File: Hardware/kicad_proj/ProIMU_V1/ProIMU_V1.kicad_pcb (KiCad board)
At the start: 2 copper layers, 50 x 50 mm, 40 parts, among them J1 USB4105-GF-A, J2 502570-0893, J3 Conn_01x01, J4 Conn_01x01, J5 Conn_01x01, J6 Conn_01x01, J7 Conn_01x01, U1 BMP280, U11 TJA1051T-3, U2 MPU-9250, U3 STM32F412CEU6, U4 AIR602

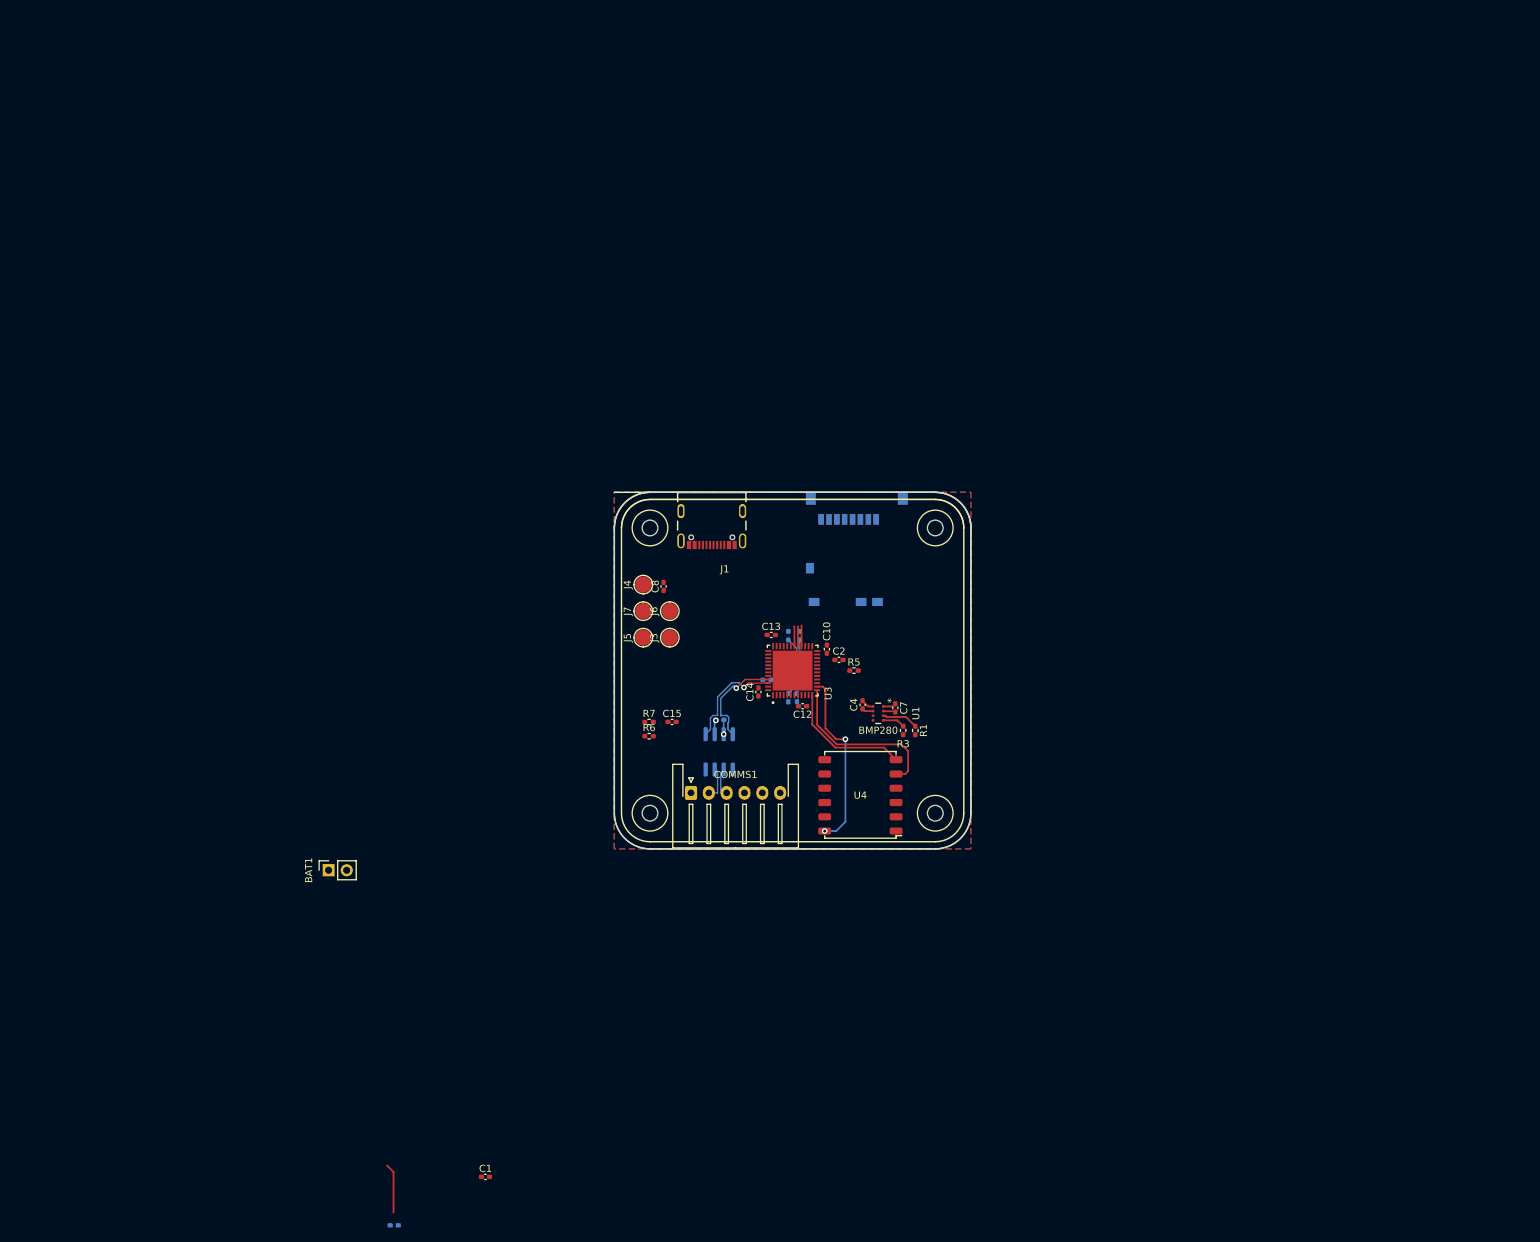
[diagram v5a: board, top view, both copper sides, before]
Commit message: Layout Updated. CAN and RS485 section to be updated
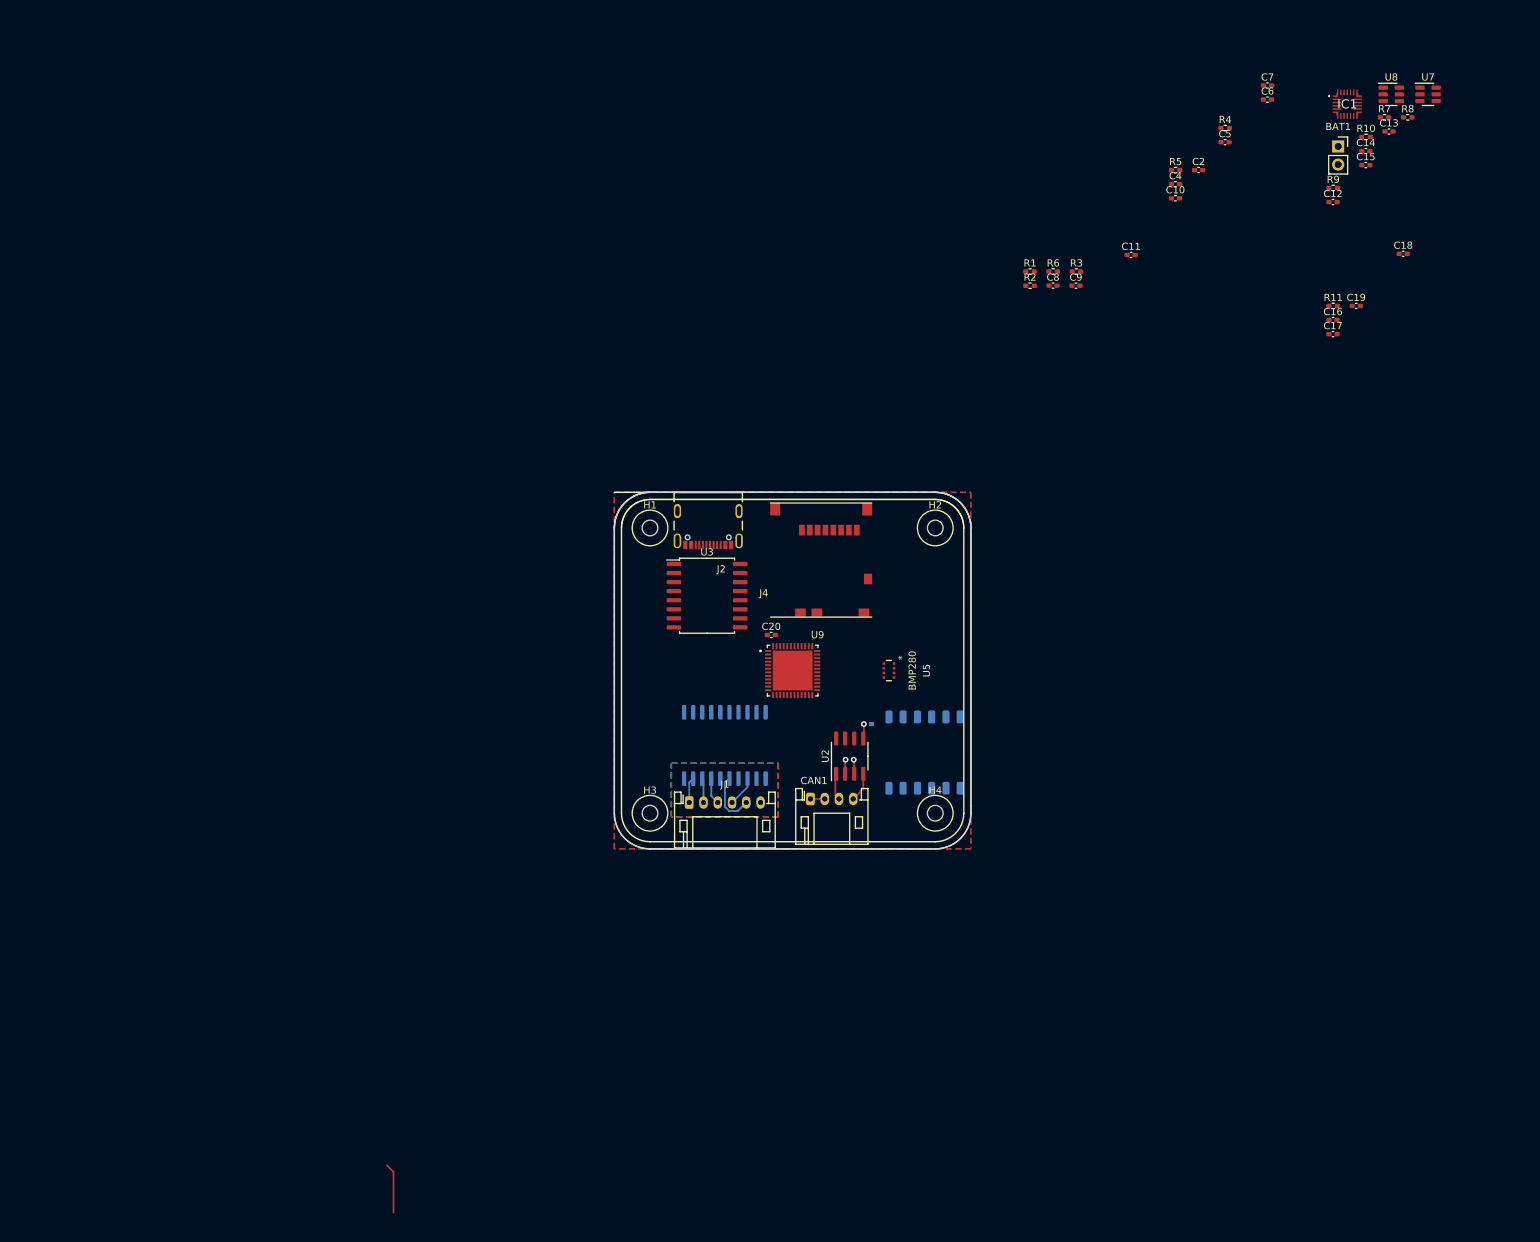
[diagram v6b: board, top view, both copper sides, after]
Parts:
- removed COMMS1: Conn_01x06, Connector_JST:JST_XH_S6B-XH-A-1_1x06_P2.50mm_Horizontal
- removed J3, J5, J6, J7: Conn_01x01, footprints:Test_Point
- removed U11: TJA1051T-3, Package_SO:SOIC-8_3.9x4.9mm_P1.27mm
- added C16: 1uF, Capacitor_SMD:C_0402_1005Metric_Pad0.74x0.62mm_HandSolder, F.Cu at (224.3, 55.9)
- added C17: 1uF, Capacitor_SMD:C_0402_1005Metric_Pad0.74x0.62mm_HandSolder, F.Cu at (224.3, 57.8)
- added C18: 1uF, Capacitor_SMD:C_0402_1005Metric_Pad0.74x0.62mm_HandSolder, F.Cu at (234.1, 46.5)
- added C19: 1uF, Capacitor_SMD:C_0402_1005Metric_Pad0.74x0.62mm_HandSolder, F.Cu at (227.5, 53.9)
- added C20: 1uF, Capacitor_SMD:C_0402_1005Metric_Pad0.74x0.62mm_HandSolder, F.Cu at (145.5, 100.0)
- added CAN1: Conn_02x02_Counter_Clockwise, Connector_JST:JST_PH_S4B-PH-K_1x04_P2.00mm_Horizontal, F.Cu at (151.0, 123.0)
- added IC1: MP2731GQC-0000-Z, footprints:MP2731GQC0000Z, F.Cu at (226.3, 25.6)
- added R10: 10K, Resistor_SMD:R_0402_1005Metric_Pad0.72x0.64mm_HandSolder, F.Cu at (228.9, 30.2)
- added R11: 10K, Resistor_SMD:R_0402_1005Metric_Pad0.72x0.64mm_HandSolder, F.Cu at (224.3, 53.9)
- added R8: 10K, Resistor_SMD:R_0402_1005Metric_Pad0.72x0.64mm_HandSolder, F.Cu at (234.8, 27.4)
- added R9: 10K, Resistor_SMD:R_0402_1005Metric_Pad0.72x0.64mm_HandSolder, F.Cu at (224.3, 37.3)
- added U5: BMP280, footprints:BMP280, F.Cu at (162.0, 105.0)
- added U6: MPU-9250, footprints:QFN40P300X300X105-24N, B.Cu at (148.5, 105.0)
- added U7: TPS54308, Package_TO_SOT_SMD:SOT-23-6, F.Cu at (237.6, 24.2)
- added U8: TPS54308, Package_TO_SOT_SMD:SOT-23-6, F.Cu at (232.4, 24.2)
- added U9: STM32F412CEU6, footprints:QFN50P700X700X60-49N, F.Cu at (148.5, 105.0)
- C1, U4: moved to B.Cu
- C10: value 1uF -> 100nF
- C11: value 1uF -> 10nF; moved to F.Cu
- C3: value 0.1uF -> 1uF
- C4: value 100nF -> 1uF
- C5: value 10nF -> 1uF; moved to F.Cu
- C6: value 0.1uF -> 100nF; moved to F.Cu
- C7: value 100nF -> 0.1uF
- C8: value 1uF -> 0.1uF
- C9, R2, R4: moved to F.Cu
- J1: value USB4105-GF-A -> Conn_01x06; footprint footprints:GCT_USB4105-GF-A -> Connector_JST:JST_PH_S6B-PH-K_1x06_P2.00mm_Horizontal
- J2: value 502570-0893 -> USB4105-GF-A; footprint footprints:MOLEX_502570-0893 -> footprints:GCT_USB4105-GF-A; moved to F.Cu
- J4: value Conn_01x01 -> 502570-0893; footprint footprints:Test_Point -> footprints:MOLEX_502570-0893
- R5: value 10K -> 2.2K
- R7: value 2.2K -> 10K
- U1: value BMP280 -> ADM2582E; footprint footprints:BMP280 -> Package_SO:SOIC-20W_7.5x12.8mm_P1.27mm; moved to B.Cu
- U2: value MPU-9250 -> TJA1051T-3; footprint footprints:QFN40P300X300X105-24N -> Package_SO:SOIC-8_3.9x4.9mm_P1.27mm; moved to F.Cu
- U3: value STM32F412CEU6 -> ADUM3160; footprint footprints:QFN50P700X700X60-49N -> Package_SO:SOIC-16W_7.5x10.3mm_P1.27mm
- moved BAT1 174.2 mm to (225.0, 31.5), turned to 0 degrees
- moved C9 162.8 mm to (188.2, 51.0)
- moved R7 133.5 mm to (231.5, 27.4)
- moved C15 124.7 mm to (228.9, 34.1)
- moved C14 114.1 mm to (228.9, 32.1), turned to 0 degrees
- moved C13 111.8 mm to (232.1, 29.4)
- moved C6 107.5 mm to (215.1, 24.9), turned to 0 degrees
- moved C12 102.6 mm to (224.3, 39.3), turned to 0 degrees
- moved C7 101.7 mm to (215.1, 23.0), turned to 0 degrees
- moved C5 98.4 mm to (209.1, 30.9), turned to 0 degrees
- moved R4 92.9 mm to (209.2, 28.9), turned to 0 degrees
- moved C11 87.0 mm to (196.0, 46.7), turned to 0 degrees
- moved R6 86.4 mm to (185.0, 49.0)
- moved C2 85.2 mm to (205.4, 34.8), turned to 0 degrees
- moved C4 85.2 mm to (202.2, 36.8), turned to 0 degrees
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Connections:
- C1 pad 1: +5V -> GND
- C1 pad 2: GND -> +3V3
- C11 pad 1: +5V -> +3V3
- C12 pad 1: +3V3 -> Net-(C12-Pad1)
- C12 pad 2: GND -> Net-(C12-Pad2)
- C13 pad 1: +3V3 -> Net-(C13-Pad1)
- C13 pad 2: GND -> Net-(C13-Pad2)
- C15 pad 1: GND -> +5V
- C15 pad 2: Net-(C15-Pad2) -> GND
- C2 pad 1: Net-(C2-Pad1) -> GND
- C2 pad 2: GND -> VDD
- C3 pad 1: +5V -> GND
- C3 pad 2: GND -> +5V
- C4 pad 1: +5V -> GND
- C4 pad 2: GND -> +3V3
- C5 pad 1: +3V3 -> GND
- C5 pad 2: GND -> Net-(C5-Pad2)
- C6 pad 1: Net-(C6-Pad1) -> GND
- C6 pad 2: GND -> +3V3
- C7 pad 1: +3V3 -> +5V
- C8 pad 1: +5V -> Net-(C8-Pad1)
- C9 pad 1: GND -> +5V
- C9 pad 2: +3V3 -> GND
- J4 pad 1: /SWCLK -> /MCU/SDCARD_D2
- R1 pad 1: /BMP280_SCL -> /MCU/CAN_L
- R1 pad 2: +3V3 -> Net-(C5-Pad2)
- R2 pad 1: /MPU9250_SCK -> Net-(C5-Pad2)
- R2 pad 2: +3V3 -> /MCU/CAN_H
- R3 pad 1: /BMP280_SDA -> /MCU/MPU9250_SDA
- R4 pad 1: /MPU9250_SDA -> /MCU/MPU9250_SCK
- R5 pad 1: +3V3 -> /MCU/BMP280_SCK
- R5 pad 2: Net-(R5-Pad2) -> +3V3
- R6 pad 1: Net-(C15-Pad2) -> /MCU/BMP280_SDA
- R6 pad 2: /CAN+ -> +3V3
- R7 pad 1: /CAN- -> Net-(R7-Pad1)
- R7 pad 2: Net-(C15-Pad2) -> +3V3
- U1 pad 3: /BMP280_SCL -> GND
- U1 pad 4: /BMP280_SDA -> /MCU/RS485_RXD
- U1 pad 5: GND -> /MCU/RS485_nRE
- U1 pad 6: +3V3 -> /MCU/RS485_DE
- U1 pad 7: GND -> /MCU/RS485_TXD
- U1 pad 8: +5V -> +3V3
- U2 pad 1: +3V3 -> Net-(CAN1-Pad3)
- U2 pad 2: (no net) -> GND
- U2 pad 3: (no net) -> +5V
- U2 pad 4: (no net) -> Net-(CAN1-Pad4)
- U2 pad 5: (no net) -> +3V3
- U2 pad 6: (no net) -> /MCU/CAN_L
- U2 pad 7: unconnected-(U2-Pad7) -> /MCU/CAN_H
- U2 pad 8: +3V3 -> /MCU/CAN_SHUTDOWN
- U3 pad 1: +BATT -> VDD
- U3 pad 10: unconnected-(U3-Pad10) -> /MCU/D+
- U3 pad 11: unconnected-(U3-Pad11) -> /MCU/D-
- U3 pad 12: /WIFI_UART_TX -> /MCU/PIN
- U3 pad 13: /WIFI_UART_RX -> /MCU/SPD
- U3 pad 14: /WIFI_RES -> +3V3
- U3 pad 15: unconnected-(U3-Pad15) -> GND
- U3 pad 16: /SDCARD_CMD -> +3V3
- U3 pad 2: unconnected-(U3-Pad2) -> Net-(J2-PadA1_B12)
- U3 pad 3: unconnected-(U3-Pad3) -> VDD
- U3 pad 4: unconnected-(U3-Pad4) -> /MCU/SPU
- U3 pad 5: unconnected-(U3-Pad5) -> /MCU/PDEN
- U3 pad 6: unconnected-(U3-Pad6) -> Net-(J2-PadA7)
- U3 pad 7: /NRST -> Net-(J2-PadA6)
- U3 pad 8: GND -> Net-(J2-PadA1_B12)
- U3 pad 9: +3V3 -> GND
- U4 pad 12: /WIFI_RES -> /MCU/WIFI_RESET
- U4 pad 5: /WIFI_UART_RX -> /MCU/WIFI_UART_TX
- U4 pad 6: /WIFI_UART_TX -> /MCU/WIFI_UART_RX
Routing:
- net /WIFI_RES: track 25.3 -> 0.00 mm, vias 2 -> 0
- net /WIFI_UART_RX: track 23.8 -> 0.00 mm
- net /WIFI_UART_TX: track 17.9 -> 0.00 mm
- net /CAN_TRX+: track 14.7 -> 0.00 mm, vias 1 -> 0
- net /CAN_TRX-: track 14.4 -> 0.00 mm, vias 1 -> 0
- net /SDCARD_CLK: track 9.89 -> 0.00 mm
- net Net-(J1-Pad5): track 0.00 -> 7.95 mm
- net (no net): track 0.00 -> 6.97 mm
- net /BMP280_SCL: track 5.09 -> 0.00 mm
- net /CAN+: track 4.64 -> 0.00 mm
- net Net-(J1-Pad4): track 0.00 -> 4.25 mm
- net /CAN-: track 4.24 -> 0.00 mm
- net Net-(CAN1-Pad4): track 0.00 -> 4.11 mm
- net Net-(CAN1-Pad3): track 0.00 -> 3.77 mm
- net Net-(J1-Pad3): track 0.00 -> 3.72 mm
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- added copper zone on B.Cu, net GND1
- added copper zone on F.Cu, net GND1

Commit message: Updated Schematic and Layout. Needs more refining
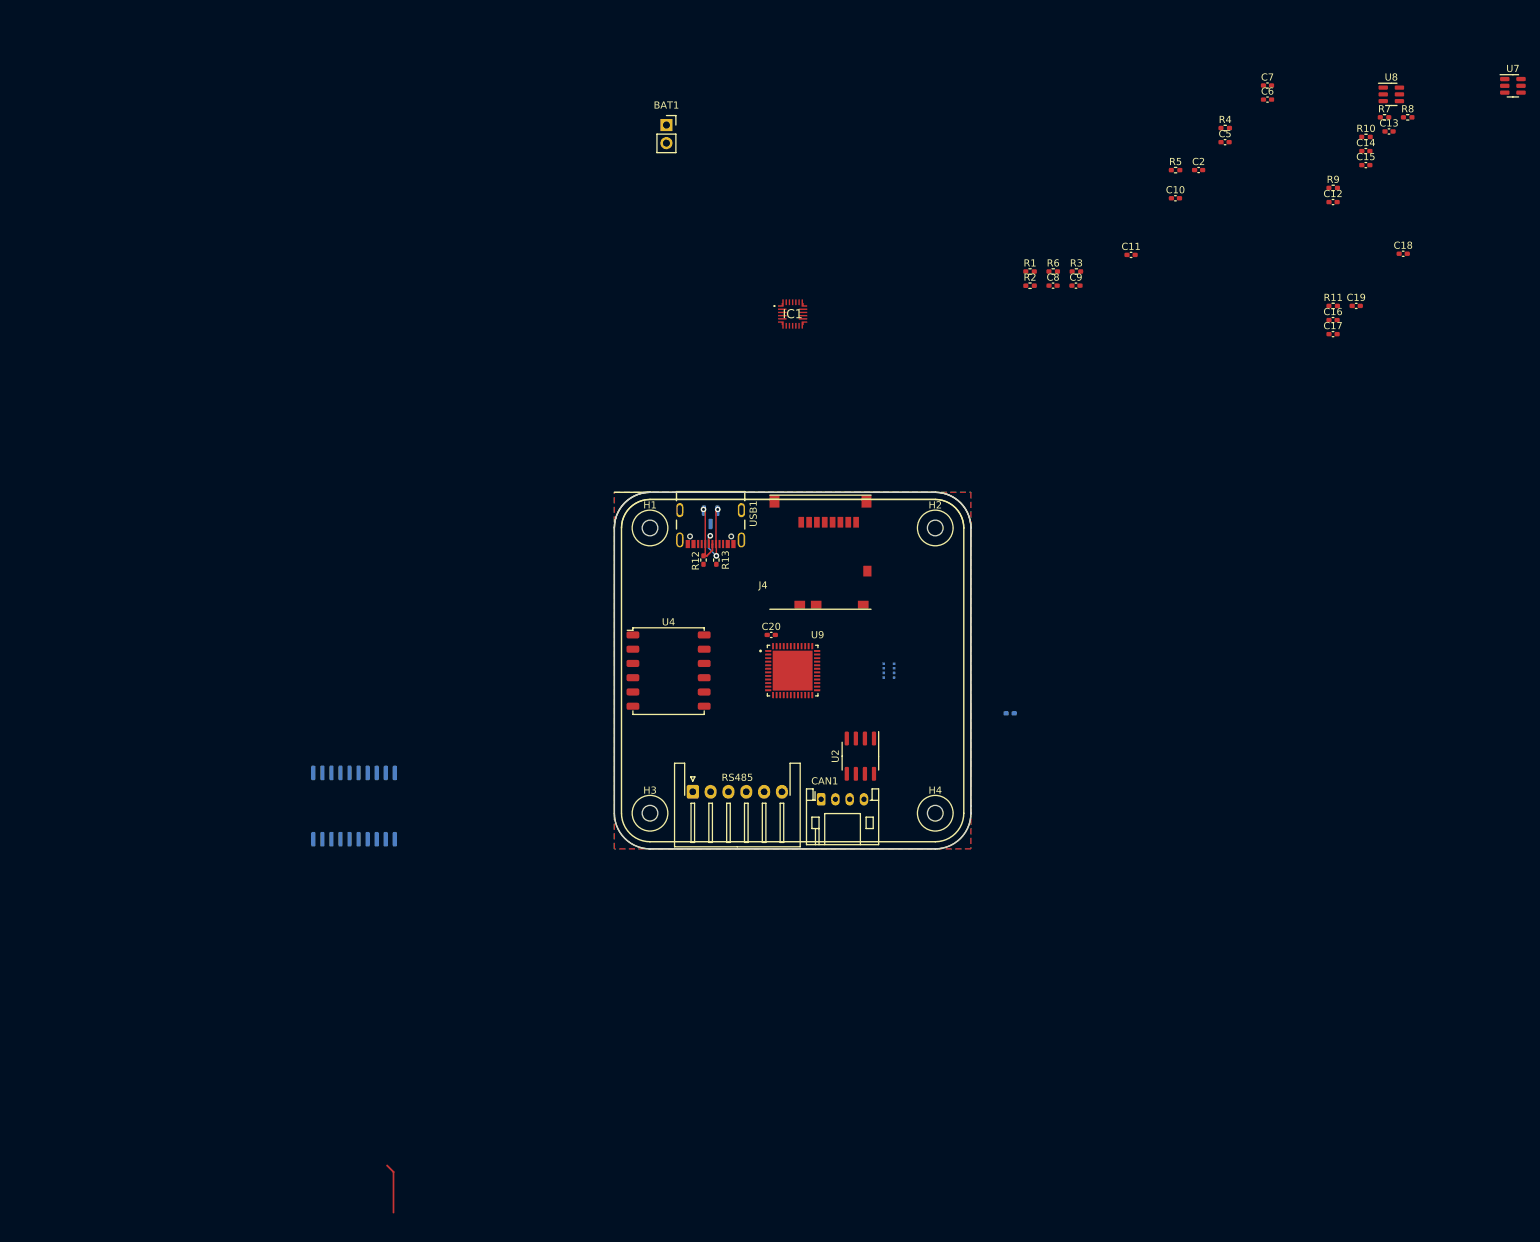
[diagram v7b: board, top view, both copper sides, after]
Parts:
- removed C1, C4: 1uF, Capacitor_SMD:C_0402_1005Metric_Pad0.74x0.62mm_HandSolder
- removed J1: Conn_01x06, Connector_JST:JST_PH_S6B-PH-K_1x06_P2.00mm_Horizontal
- removed J2: USB4105-GF-A, footprints:GCT_USB4105-GF-A
- removed U3: ADUM3160, Package_SO:SOIC-16W_7.5x10.3mm_P1.27mm
- added D1: SP0502BAHT, Package_TO_SOT_SMD:SOT-23, B.Cu at (137.0, 83.5)
- added R12: 22R, Resistor_SMD:R_0402_1005Metric_Pad0.72x0.64mm_HandSolder, F.Cu at (136.0, 89.5)
- added R13: 22R, Resistor_SMD:R_0402_1005Metric_Pad0.72x0.64mm_HandSolder, F.Cu at (137.8, 89.5)
- added RS485: 43045-0609, Connector_JST:JST_XH_S6B-XH-A-1_1x06_P2.50mm_Horizontal, F.Cu at (134.5, 122.0)
- added USB1: USB4105-GF-A, footprints:GCT_USB4105-GF-A, F.Cu at (137.0, 82.5)
- CAN1: value Conn_02x02_Counter_Clockwise -> Conn_01x04
- U4: moved to F.Cu
- U5: moved to B.Cu
- moved BAT1 94.2 mm to (130.8, 28.5)
- moved IC1 83.2 mm to (148.5, 55.0)
- moved U1 52.7 mm to (87.0, 124.0)
- moved U4 37.7 mm to (131.1, 105.0), turned to 0 degrees
- moved C3 23.4 mm to (179.0, 111.0)
- moved U7 12.0 mm to (249.5, 23.0)
- moved CAN1 1.50 mm to (152.5, 123.0)
- moved U2 1.50 mm to (158.0, 117.0), turned to -90 degrees
- moved J4 1.10 mm to (152.4, 88.4)
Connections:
- CAN1 pad 2: GND -> Net-(R1-Pad1)
- CAN1 pad 3: Net-(CAN1-Pad3) -> Net-(R2-Pad2)
- CAN1 pad 4: Net-(CAN1-Pad4) -> GND
- R1 pad 1: /MCU/CAN_L -> Net-(R1-Pad1)
- R2 pad 2: /MCU/CAN_H -> Net-(R2-Pad2)
- U2 pad 1: Net-(CAN1-Pad3) -> /MCU/CAN_TX
- U2 pad 4: Net-(CAN1-Pad4) -> /MCU/CAN_RX
- U2 pad 6: /MCU/CAN_L -> Net-(R1-Pad1)
- U2 pad 7: /MCU/CAN_H -> Net-(R2-Pad2)
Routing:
- net /D1-: track 0.00 -> 11.2 mm, vias 0 -> 3
- net /D1+: track 0.00 -> 9.19 mm, vias 0 -> 1
- net Net-(RS485-Pad5): track 7.95 -> 0.00 mm
- net Net-(RS485-Pad4): track 4.25 -> 0.00 mm
- net Net-(CAN1-Pad4): track 4.11 -> 0.00 mm
- net GND: track 4.00 -> 0.00 mm, vias 1 -> 0
- net Net-(CAN1-Pad3): track 3.77 -> 0.00 mm
- net Net-(RS485-Pad3): track 3.72 -> 0.00 mm
- net Net-(RS485-Pad1): track 3.58 -> 0.00 mm
- net Net-(RS485-Pad2): track 3.42 -> 0.00 mm
- net +3V3: track 2.06 -> 0.00 mm, vias 1 -> 0
- net +5V: track 2.00 -> 0.00 mm, vias 1 -> 0
- removed copper zone on B.Cu, net GND1
- removed copper zone on F.Cu, net GND1
